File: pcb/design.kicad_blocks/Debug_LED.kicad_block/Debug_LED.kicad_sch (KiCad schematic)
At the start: 4 parts

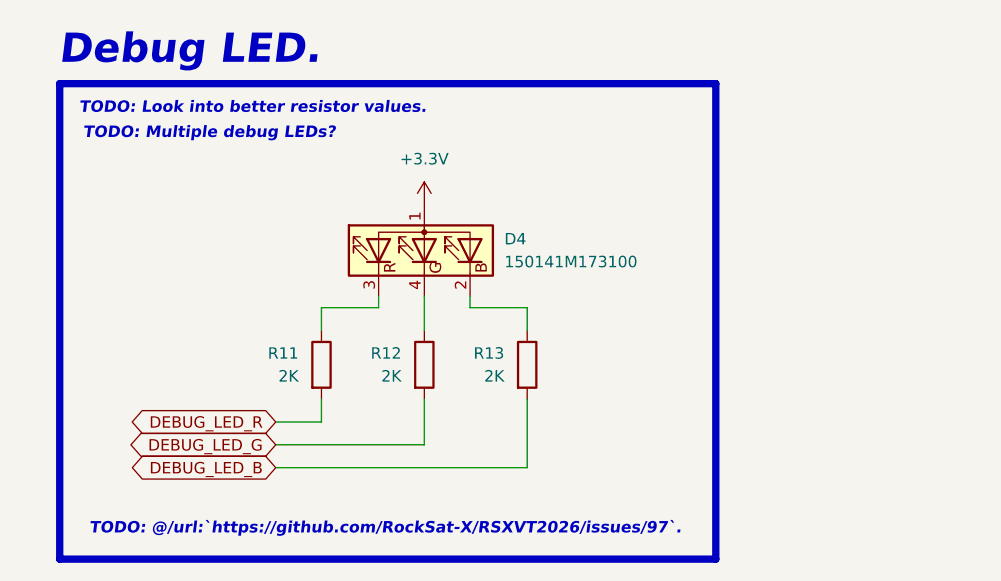
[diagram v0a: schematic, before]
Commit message: Added debug LED pins.
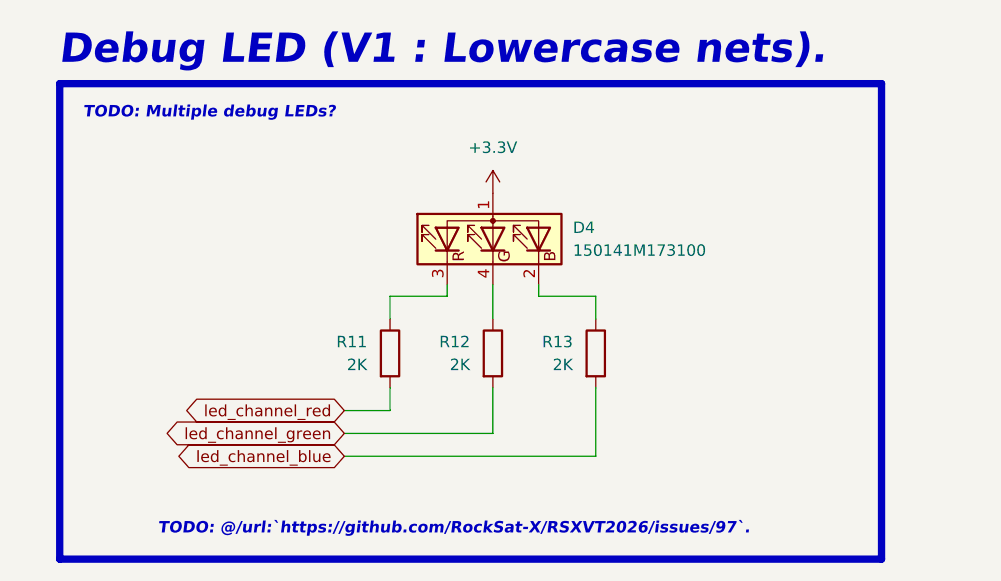
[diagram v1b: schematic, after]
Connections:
- net DEBUG_LED_B renamed led_channel_blue
- net DEBUG_LED_G renamed led_channel_green
- net DEBUG_LED_R renamed led_channel_red
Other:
- note added: "Debug LED (V1 : Lowercase nets)."
- note removed: "Debug LED."
- note removed: "TODO: Look into better resistor values."
- moved on the sheet: D4, R11, R12, R13

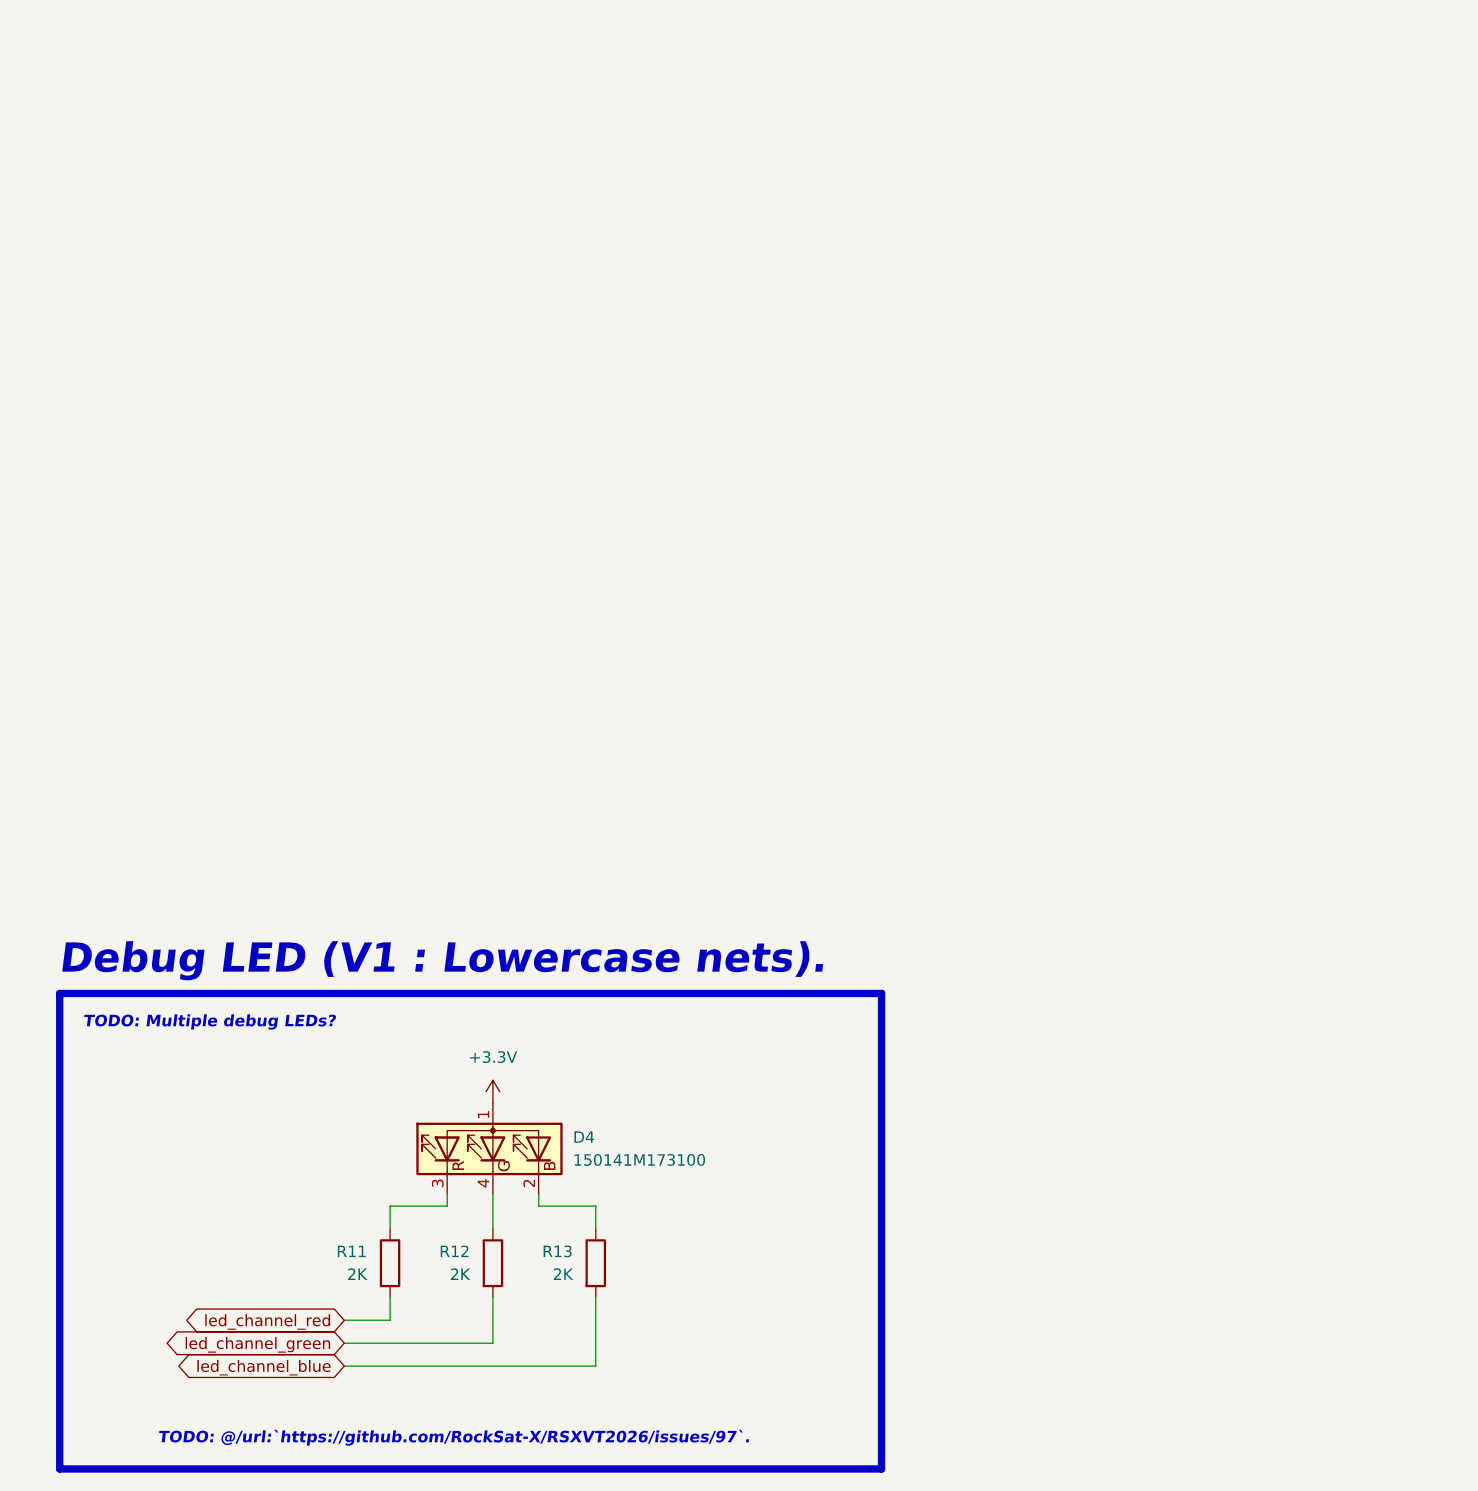
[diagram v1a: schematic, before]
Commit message: Placed down most of the components.
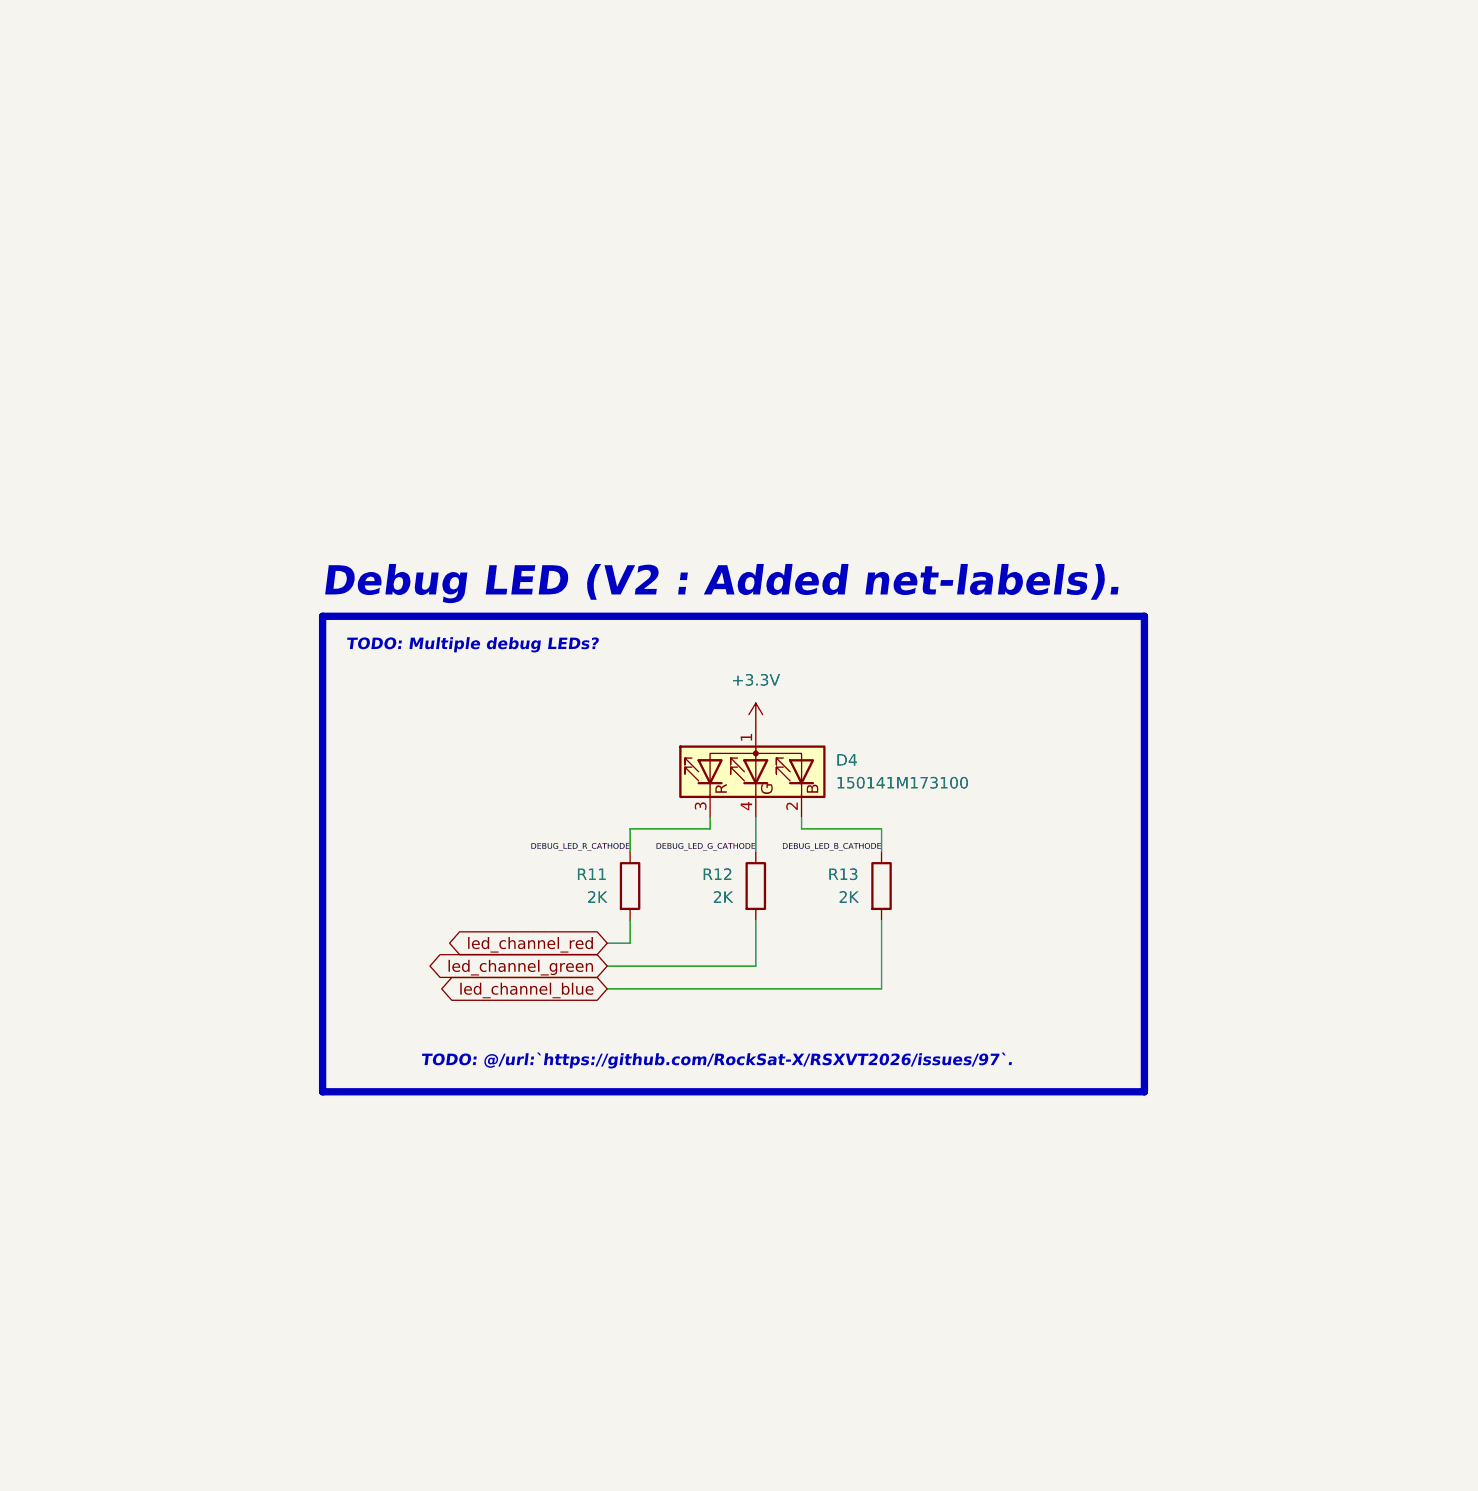
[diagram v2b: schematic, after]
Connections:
- net DEBUG_LED_G_CATHODE: now reaches D4.4 (GK), R12.1
- net DEBUG_LED_B_CATHODE: now reaches D4.2 (BK), R13.1
- net DEBUG_LED_R_CATHODE: now reaches D4.3 (RK), R11.1
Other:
- note added: "Debug LED (V2 : Added net-labels)."
- note removed: "Debug LED (V1 : Lowercase nets)."
- moved on the sheet: D4, R11, R12, R13

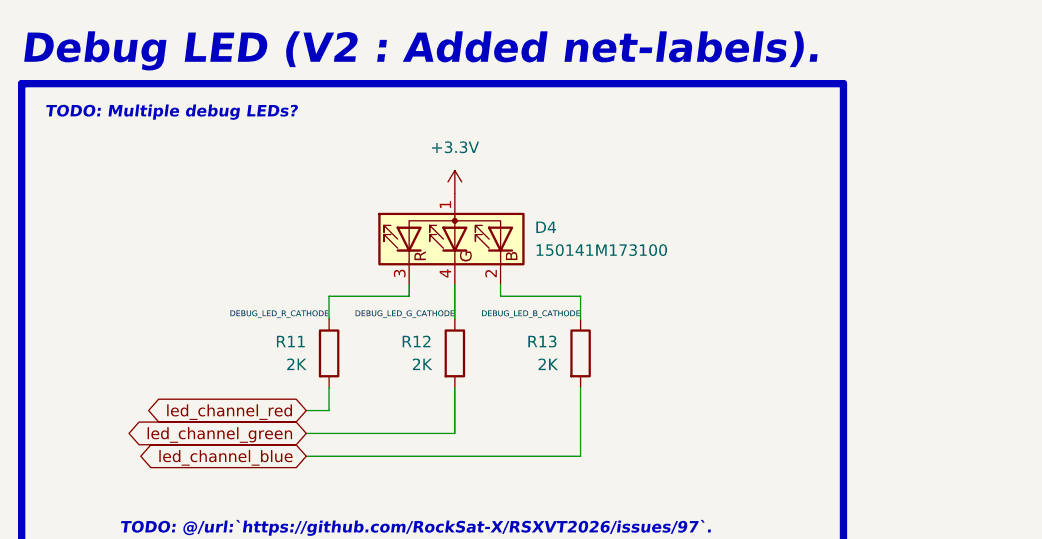
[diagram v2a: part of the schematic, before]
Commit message: Updated design blocks of debug buzzer and debug led.
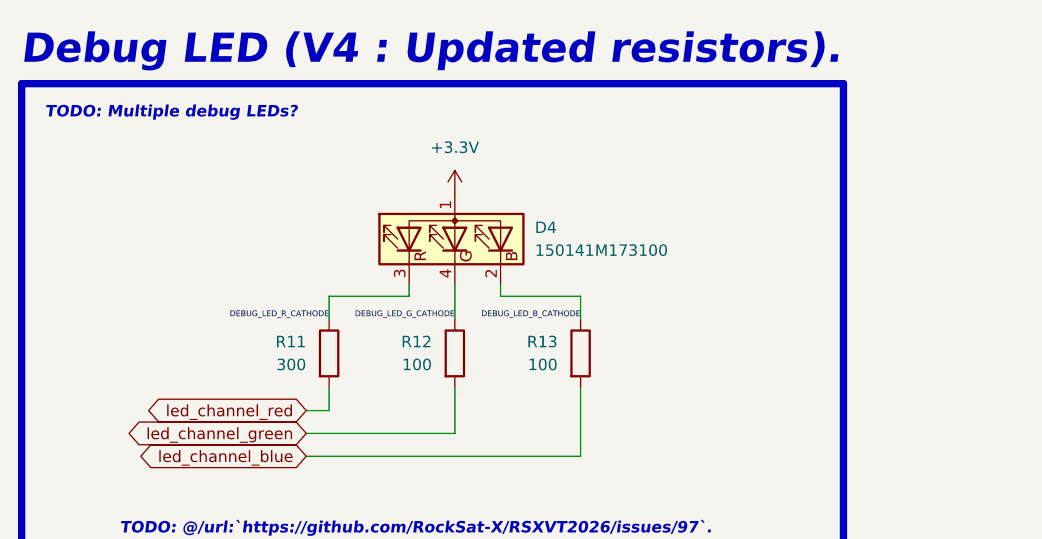
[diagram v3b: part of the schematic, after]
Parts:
- R11: value 2K -> 300
- R12, R13: value 2K -> 100
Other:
- note added: "Debug LED (V4 : Updated resistors)."
- note removed: "Debug LED (V2 : Added net-labels)."
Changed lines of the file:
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@@
 		)
 	)
-	(text "Debug LED (V2 : Added net-labels)."
+	(text "Debug LED (V4 : Updated resistors)."
 		(exclude_from_sim no)
 		(at 450.85 224.79 0)
@@
 			)
 		)
-		(property "Value" "2K"
+		(property "Value" "100"
 			(at 496.57 257.8099 0)
 			(effects
@@
 			)
 		)
-		(property "Value" "2K"
+		(property "Value" "100"
 			(at 510.54 257.8099 0)
 			(effects
@@
 			)
 		)
-		(property "Value" "2K"
+		(property "Value" "300"
 			(at 482.6 257.8099 0)
 			(effects
